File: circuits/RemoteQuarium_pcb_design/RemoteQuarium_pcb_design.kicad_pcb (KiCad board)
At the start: 2 copper layers, 53 parts, among them J1 Power_terminal, J10 LCD_pins, J11 Servo pins, J12 ESP_pins, J13 PH_sensor_sockets, J14 Ph_sesnor-pins, J15 Power & RX-TX, J16 Reset_button_terminal, J2 ESP left side sockets, J3 ESP right side sockets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

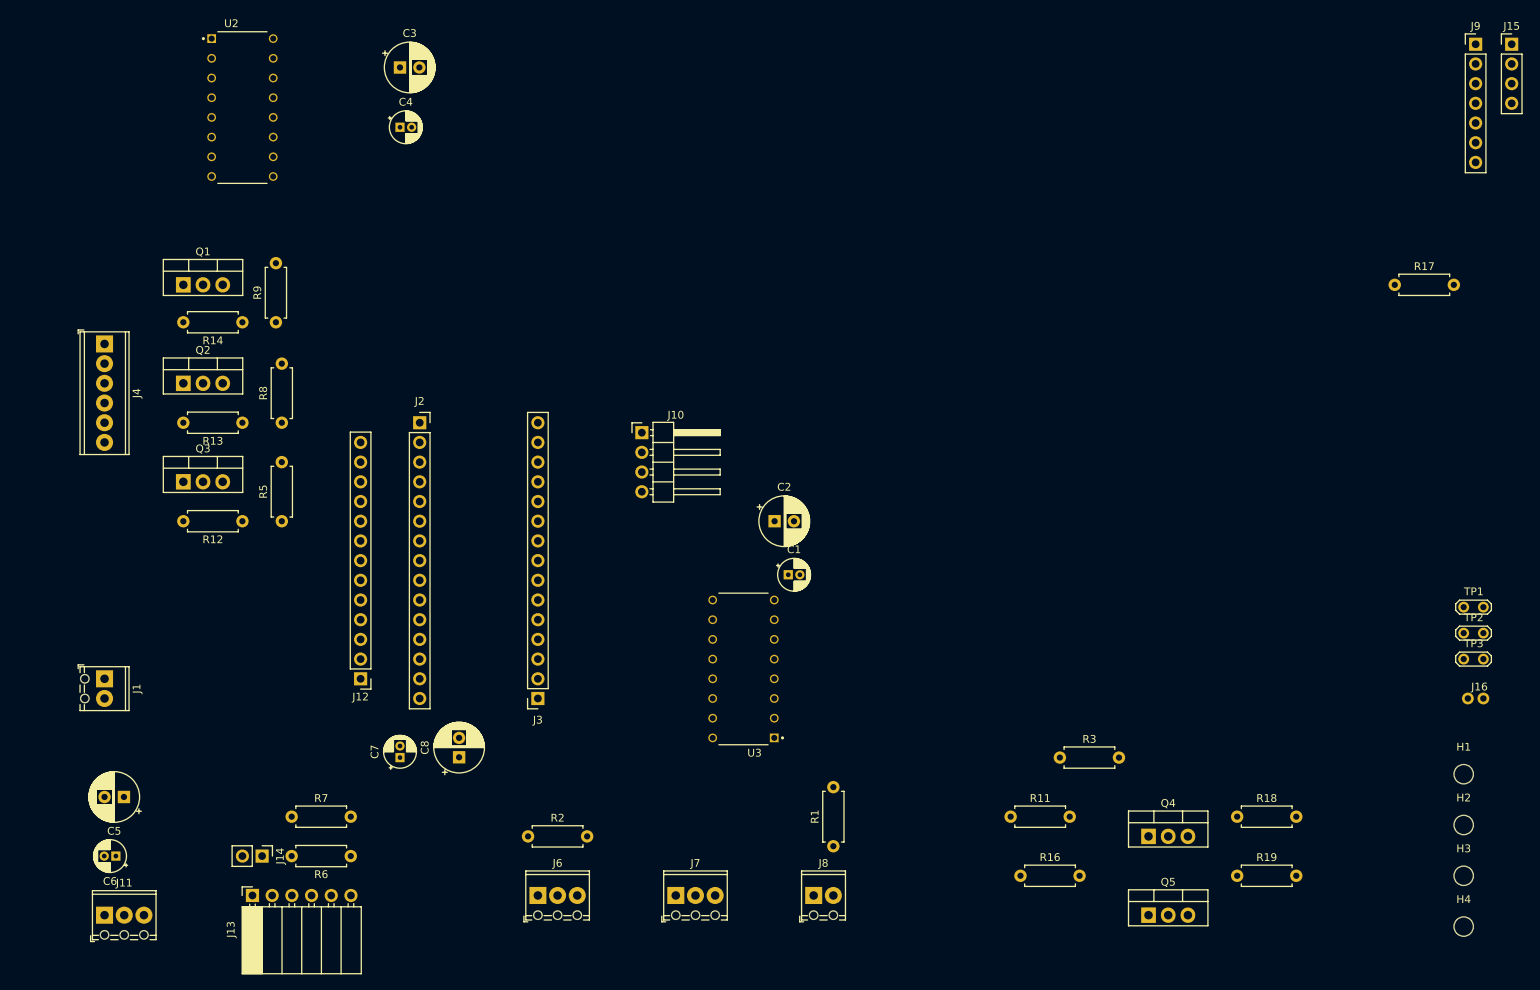
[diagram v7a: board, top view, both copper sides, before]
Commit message: Fixed user email change issue
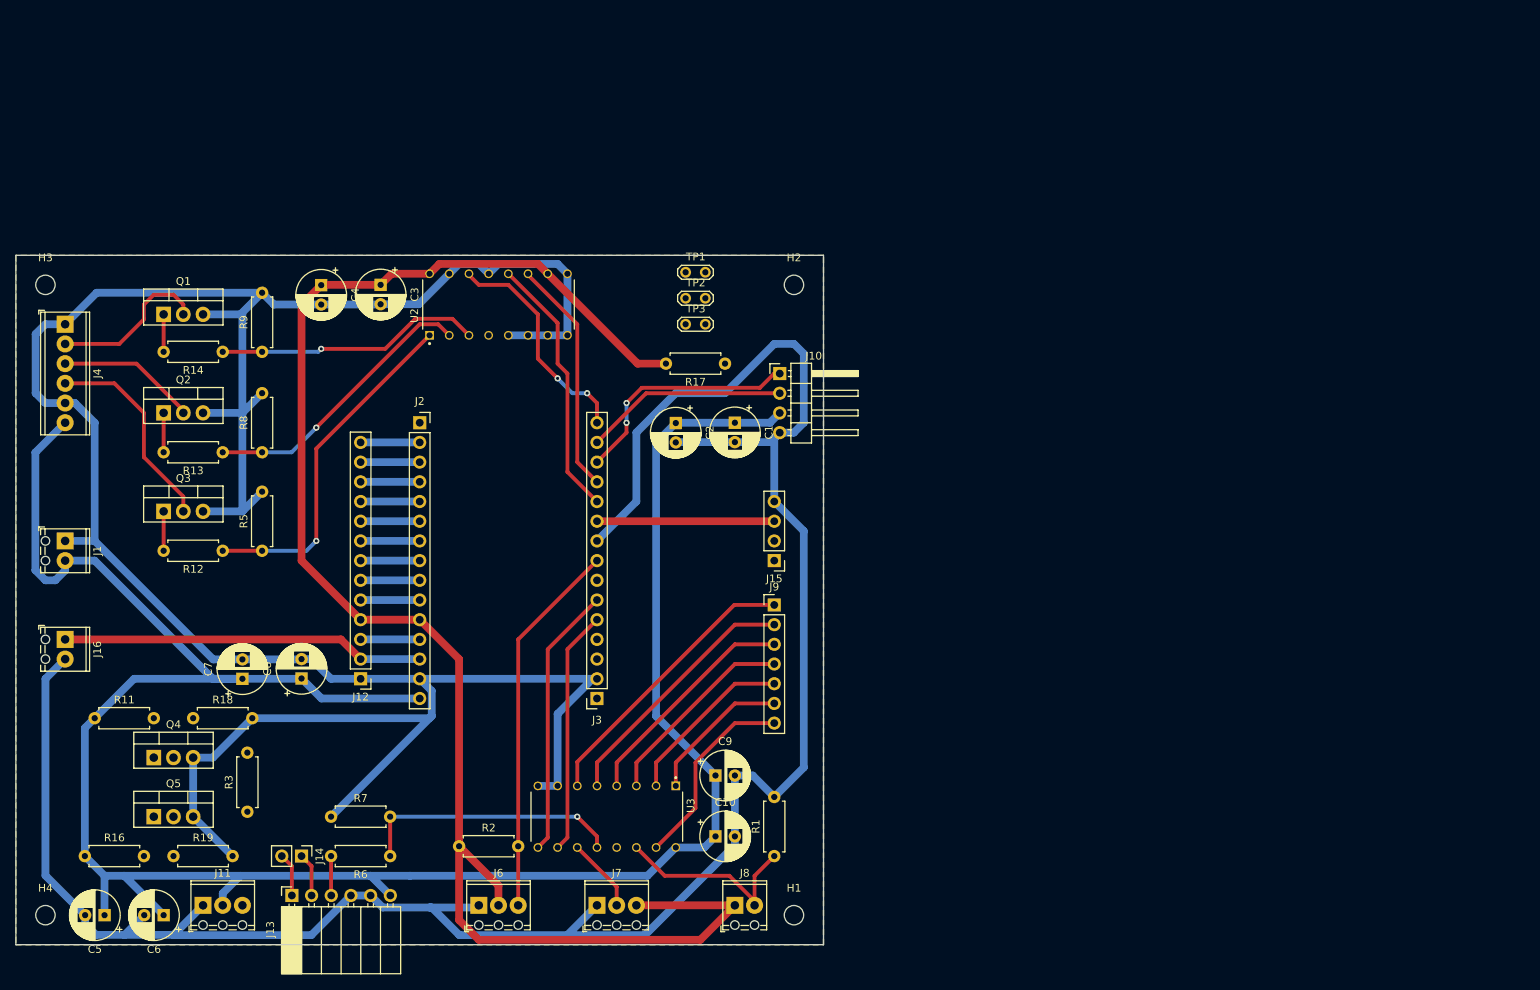
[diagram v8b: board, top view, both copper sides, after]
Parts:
- added C10: 10uF, Capacitor_THT:CP_Radial_D6.3mm_P2.50mm, F.Cu at (167.7, 134.6)
- added C9: 0.1uF, Capacitor_THT:CP_Radial_D6.3mm_P2.50mm, F.Cu at (167.7, 126.8)
- C1, C4, C6, C7: footprint Capacitor_THT:CP_Radial_D4.0mm_P1.50mm -> Capacitor_THT:CP_Radial_D6.3mm_P2.50mm
- J16: footprint NXW:NXW-02P -> TerminalBlock_Phoenix:TerminalBlock_Phoenix_MPT-0,5-2-2.54_1x02_P2.54mm_Horizontal
- moved H3 198.1 mm to (81.3, 63.5)
- moved H4 182.9 mm to (81.3, 144.8)
- moved J16 181.0 mm to (83.8, 109.2), turned to -90 degrees
- moved R19 137.2 mm to (97.8, 137.2)
- moved R18 135.2 mm to (100.3, 119.4)
- moved Q5 128.9 mm to (95.2, 132.1)
- moved Q4 128.7 mm to (95.2, 124.5)
- moved R16 120.7 mm to (86.4, 137.2)
- moved R11 118.8 mm to (87.6, 119.4)
- moved J15 116.1 mm to (175.3, 99.1), turned to 180 degrees
- moved J9 115.8 mm to (175.3, 104.8)
- moved H2 110.9 mm to (177.8, 63.5)
- moved TP1 109.2 mm to (163.8, 61.9)
- moved TP2 109.2 mm to (163.8, 65.2)
- moved TP3 109.2 mm to (163.8, 68.6)
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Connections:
- net /D35V renamed /D65V
- C1 pad 1: Earth -> /VIN
- C1 pad 2: /VIN -> /GND
- C2 pad 1: Earth -> /VIN
- C2 pad 2: /VIN -> /GND
- C3 pad 1: Earth -> /VCC
- C3 pad 2: /VCC -> /GND
- C4 pad 1: Earth -> /VCC
- C4 pad 2: /VCC -> /GND
- C5 pad 2: Earth -> /GND
- C6 pad 2: Earth -> /GND
- C7 pad 1: Earth -> /VIN
- C7 pad 2: /VIN -> /GND
- C8 pad 1: Earth -> /VIN
- C8 pad 2: /VIN -> /GND
- J1 pad 1: Earth -> /GND
- J10 pad 4: Earth -> /GND
- J11 pad 1: Earth -> /GND
- J12 pad 1: Earth -> /GND
- J12 pad 5: Earth -> /GND
- J13 pad 4: Earth -> /GND
- J13 pad 5: Earth -> /GND
- J15 pad 4: Earth -> /GND
- J16 pad 2: Earth -> /GND
- J2 pad 10: Earth -> /GND
- J2 pad 14: Earth -> /GND
- J3 pad 2: Earth -> /GND
- J3 pad 9: Earth -> /GND
- J4 pad 1: Earth -> /GND
- J4 pad 5: Earth -> /GND
- J6 pad 1: Earth -> /GND
- J6 pad 3: /D4 -> /D5
- J7 pad 1: Earth -> /GND
- J9 pad 1: /Y -> /INH
- J9 pad 2: /INH -> /Y1
- J9 pad 3: /X3 -> /Y3
- J9 pad 4: /Y3 -> /Y
- J9 pad 6: /Y1 -> /Y0
- J9 pad 7: /Y0 -> /X3
- Q1 pad 3: Earth -> /GND
- Q2 pad 3: Earth -> /GND
- Q3 pad 3: Earth -> /GND
- Q4 pad 3: Earth -> /GND
- Q5 pad 3: Earth -> /GND
- R1 pad 2: Earth -> /GND
- R18 pad 2: Earth -> /GND
- R19 pad 2: Earth -> /GND
- R2 pad 2: /D4 -> /D5
- R3 pad 1: /D3 -> /D6
- R5 pad 2: Earth -> /GND
- R7 pad 1: Earth -> /GND
- R8 pad 2: Earth -> /GND
- R9 pad 2: Earth -> /GND
- TP1 pad 1: Earth -> /GND
- U2 pad 11: /D5 -> /D3
- U2 pad 12: /D6 -> /D4
- U2 pad 13: Earth -> /GND
- U2 pad 15: Earth -> /GND
- U2 pad 4: Earth -> /R_LED
- U2 pad 5: /R_LED -> /GND
- U2 pad 6: Earth -> /GND
- U2 pad 7: Earth -> /GND
- U2 pad 8: Earth -> /GND
- U2 pad 9: Earth -> /GND
- U3 pad 11: /X3 -> /WATER_DAT
- U3 pad 15: /WATER_DAT -> /X3
- U3 pad 7: Earth -> /GND
- U3 pad 8: Earth -> /GND
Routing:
- net /GND: track 0.00 -> 634.9 mm
- net /VIN: track 0.00 -> 296.0 mm
- net /VCC: track 0.00 -> 230.5 mm
- net /A0: track 0.00 -> 69.8 mm
- net /D5: track 0.00 -> 48.7 mm
- net /RST: track 0.00 -> 46.8 mm
- net /S0: track 0.00 -> 45.2 mm, vias 0 -> 1
- net /INH: track 0.00 -> 36.9 mm
- net /S1: track 0.00 -> 36.6 mm, vias 0 -> 1
- net /D7: track 0.00 -> 35.1 mm
- net /S2: track 0.00 -> 34.4 mm, vias 0 -> 1
- net /P0R: track 0.00 -> 34.2 mm, vias 0 -> 1
- net /D4: track 0.00 -> 34.1 mm
- net /Y1: track 0.00 -> 33.2 mm
- net /D8: track 0.00 -> 31.5 mm
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- added copper zone on B.Cu, net /GND
- added copper zone on F.Cu, net /GND
- added copper zone on In1.Cu, net /GND
- added copper zone on In2.Cu, net /GND
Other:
- board outline added: 104.1 x 88.9 mm
- copper layers 2 -> 4
